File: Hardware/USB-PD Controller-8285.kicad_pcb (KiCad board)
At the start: 2 copper layers, 34 x 34 mm, 30 parts, among them J1 Conn_01x07_Male, J10 Conn_Coaxial, J2 Conn_01x04_Male, J3 Conn_01x02_Male, J4 Conn_01x02_Male, J5 Conn_01x02_Male, J6 Conn_01x02_Male, J7 Conn_01x08_Male, Q1 UMH3N, U1 ESP8285H16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

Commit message: messin' with the controller board
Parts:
- added J8: QWIIC, Connector_JST:JST_SH_BM04B-SRSS-TB_1x04-1MP_P1.00mm_Vertical, F.Cu at (91.4, 93.7)
- moved G*** 17.6 mm to (90.4, 72.9)
- moved REF** 16.6 mm to (108.0, 73.5)
- moved C5 1.36 mm to (92.3, 87.8), turned to 180 degrees
- moved C8 1.00 mm to (87.8, 80.0)
- moved R6 0.06 mm to (94.9, 98.4)
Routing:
- net SDA: track 12.8 -> 24.7 mm
- net SCL: track 17.8 -> 26.4 mm
- net RST: track 31.9 -> 39.2 mm
- net +3V3: track 84.0 -> 89.7 mm, vias 3 -> 4
- net IO0: track 21.5 -> 23.0 mm
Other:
- board text added: "(AFC)"

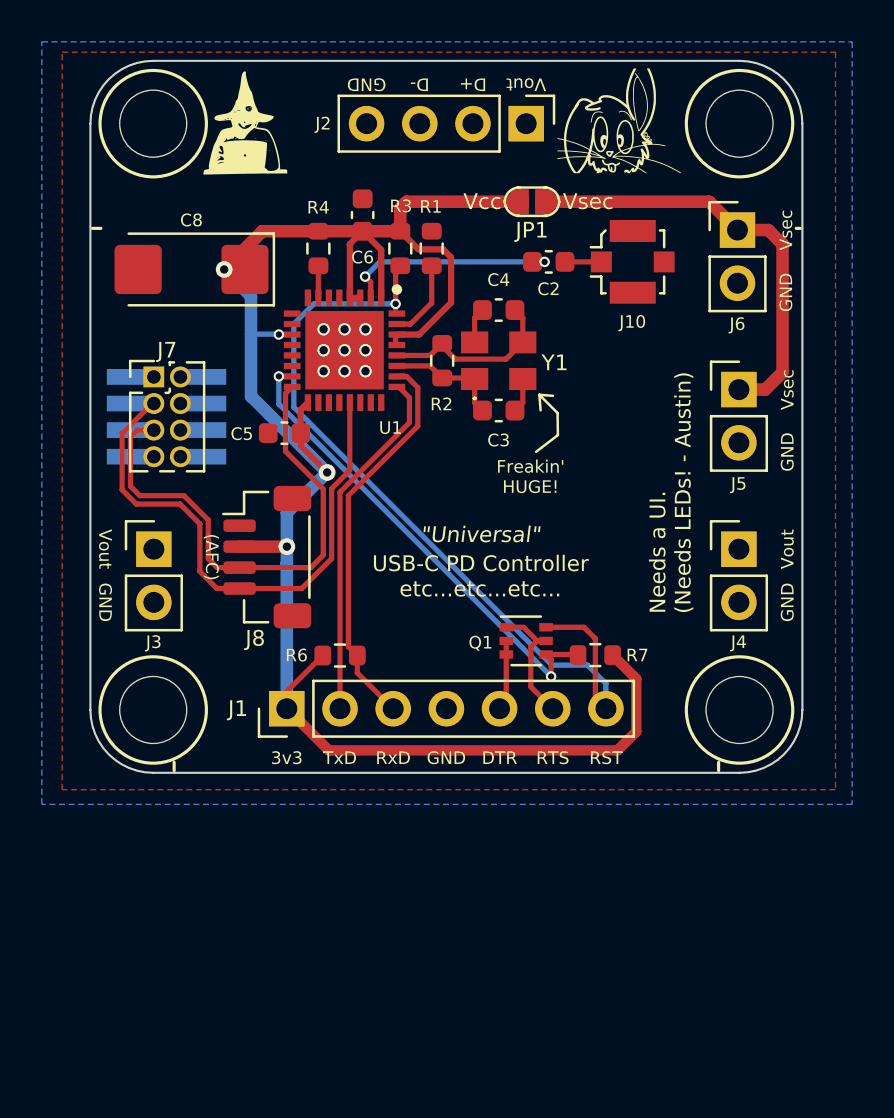
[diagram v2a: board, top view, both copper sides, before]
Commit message: aaarrrggg... RABBITS! Now there's a programmer board.
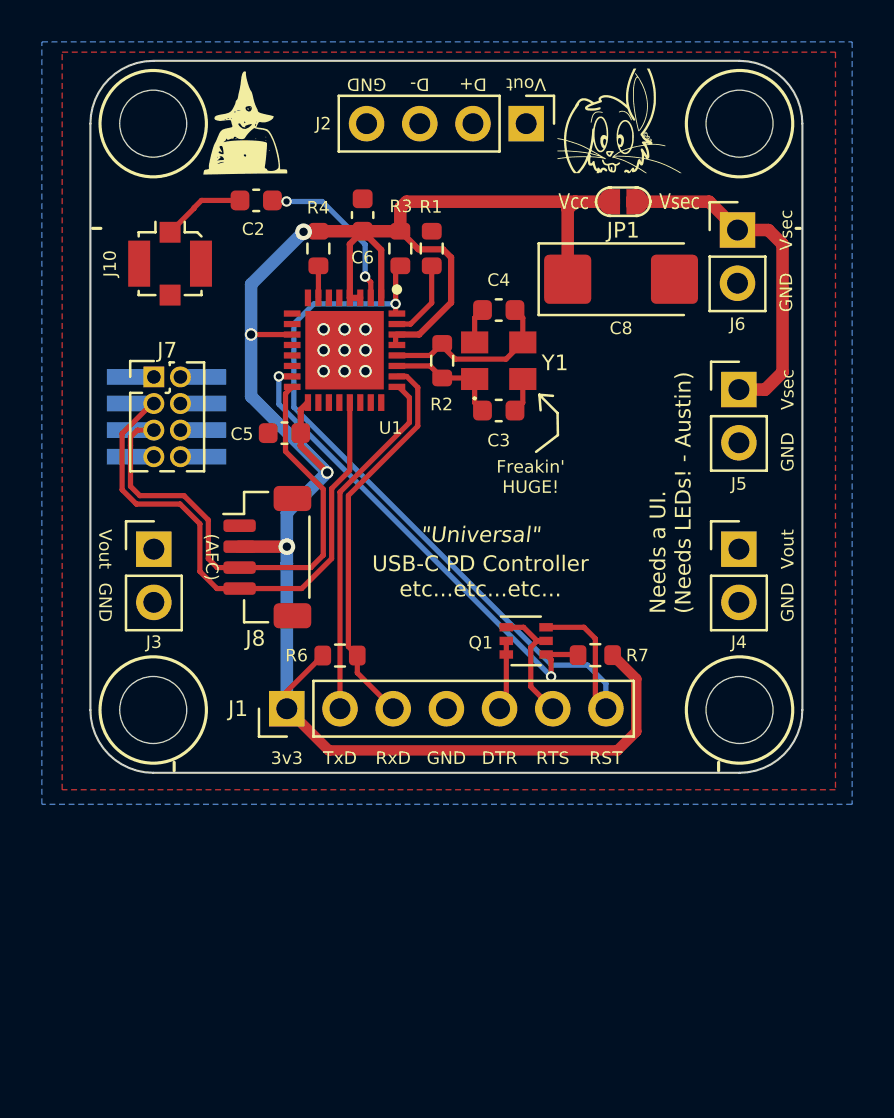
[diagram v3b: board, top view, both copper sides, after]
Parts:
- moved J10 22.1 mm to (86.8, 79.7), turned to 180 degrees
- moved C8 20.5 mm to (108.3, 80.4), turned to 0 degrees
- moved C2 14.3 mm to (90.9, 76.7), turned to 180 degrees
- moved JP1 4.36 mm to (108.4, 76.7)
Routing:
- net +3V3: track 89.7 -> 94.9 mm
- net Vsec: track 20.7 -> 16.3 mm
- net /LNA: track 9.99 -> 7.27 mm
- net Net-(C2-Pad2): track 1.73 -> 3.98 mm

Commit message: Documentation...
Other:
- board text added: "QWIIC"
- board text removed: "(AFC)"
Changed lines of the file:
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@@
     (property "exclude_from_bom" "")
     (attr smd exclude_from_bom)
-    (fp_text reference "J10" (at 2.869224 0 90) (layer "F.SilkS")
+    (fp_text reference "J10" (at -0.020454 2.740556 180) (layer "F.SilkS")
       (effects (font (size 0.6 0.6) (thickness 0.15)))
     )
@@
     (attr smd)
     (fp_text reference "Y1" (at 2.687129 0.106632) (layer "F.SilkS")
-      (effects (font (size 0.75 0.75) (thickness 0.1875)))
+      (effects (font (size 0.6 0.6) (thickness 0.15)))
     )
     (fp_text value "26.000MHz" (at 0 0.225) (layer "F.SilkS") hide
@@
     (effects (font (size 0.6 0.6) (thickness 0.125)))
   )
-  (gr_text "(AFC)" (at 88.8 93.7 270) (layer "F.SilkS")
+  (gr_text "QWIIC" (at 88.8 93.7 270) (layer "F.SilkS")
     (effects (font (size 0.6 0.6) (thickness 0.15)))
   )

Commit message: Tinkerin' + RESET & LED on Programmer...
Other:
- board text added: "NerdMage Modules ${TITLE} (v${REVISION})"
- board text removed: "NerdMage Modules (v0.0.1)"
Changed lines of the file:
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@@
   (paper "A4")
   (title_block
-    (title "USB-C PD Controller")
-    (rev "0.0.1")
+    (title "USB-PD Controller")
+    (rev "0.0.2")
     (company "The Nerd Mage")
   )
@@
   (gr_line (start 86 104) (end 114 104) (layer "Edge.Cuts") (width 0.1))
   (gr_arc (start 117 101) (mid 116.12132 103.12132) (end 114 104) (layer "Edge.Cuts") (width 0.1))
-  (gr_text "NerdMage Modules (v0.0.1)" (at 100 74.8) (layer "B.SilkS")
+  (gr_text "NerdMage Modules\n${TITLE} (v${REVISION})" (at 100 76) (layer "B.SilkS")
     (effects (font (size 1 1) (thickness 0.15)) (justify mirror))
   )
@@
     (effects (font (size 0.6 0.6) (thickness 0.125)) (justify mirror))
   )
-  (gr_text "S. A. Miller 2023" (at 100 99) (layer "B.SilkS")
+  (gr_text "S. A. Miller 2023" (at 100 79) (layer "B.SilkS")
     (effects (font (size 1 1) (thickness 0.15)) (justify mirror))
   )

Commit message: Expanding on the Controller Board functionality...
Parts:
- removed J8: QWIIC, Connector_JST:JST_SH_BM04B-SRSS-TB_1x04-1MP_P1.00mm_Vertical
- added J9: QWIIC_Stackable, Tinker:QWIIC_Stackable, F.Cu at (87.0, 80.0)
- added SW1: SW_Push, Tinker:SW_Push_TS273014TP, F.Cu at (109.0, 93.3)
- moved J10 23.4 mm to (109.0, 87.0)
- moved C2 18.5 mm to (108.2, 83.1), turned to 0 degrees
- moved C5 1.07 mm to (91.2, 87.7), turned to -90 degrees
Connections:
- J7 pad 1: RESET -> IO16
- J7 pad 4: POWER_OK2 -> IO12
- J7 pad 6: POWER_OK3 -> IO13
- J7 pad 8: GPIO -> PD_GPIO
- U1 pad 13: IO15 -> PD_GPIO
- U1 pad 14: IO2 -> ALERT
- U1 pad 21: SCL -> IO6
- U1 pad 24: IO5 -> SCL
- U1 pad 9: IO14 -> ATTACH
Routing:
- net Vsec: track 16.3 -> 31.2 mm
- net ALERT: track 0.00 -> 14.0 mm, vias 0 -> 1
- net PD_GPIO: track 0.00 -> 12.9 mm, vias 0 -> 1
- net IO16: track 0.00 -> 10.3 mm, vias 0 -> 1
- net IO13: track 0.00 -> 9.20 mm, vias 0 -> 2
- net /LNA: track 7.27 -> 16.3 mm
- net IO12: track 0.00 -> 8.43 mm, vias 0 -> 2
- net ATTACH: track 0.00 -> 7.60 mm, vias 0 -> 1
- net RST: track 39.2 -> 46.7 mm
- net IO0: track 23.0 -> 28.6 mm
- net SDA: track 24.7 -> 19.6 mm
- net +3V3: track 94.9 -> 92.1 mm, vias 4 -> 3
- net SCL: track 26.4 -> 23.9 mm
- net Net-(C2-Pad2): track 3.98 -> 2.35 mm
- net GND: vias 9 -> 1
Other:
- board text added: "RESET"
- board text added: "alert"
- board text added: "attach"
- board text added: "gpio"
- board text added: "pok2"
- board text added: "pok3"
- board text added: "rst"
- board text added: "scl"
- board text added: "sda"
- board text added: "xxxxxx"

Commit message: ...
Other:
- board text added: "${TITLE}"
- board text removed: "USB-C PD Controller etc...etc...etc..."
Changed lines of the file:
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@@
     (effects (font (size 1 1) (thickness 0.15)))
   )
-  (gr_text "USB-C PD Controller\netc...etc...etc..." (at 94.437347 93.027774 45) (layer "F.SilkS")
+  (gr_text "${TITLE}" (at 94.437347 93.027774 45) (layer "F.SilkS")
     (effects (font (size 0.75 0.75) (thickness 0.15)))
   )

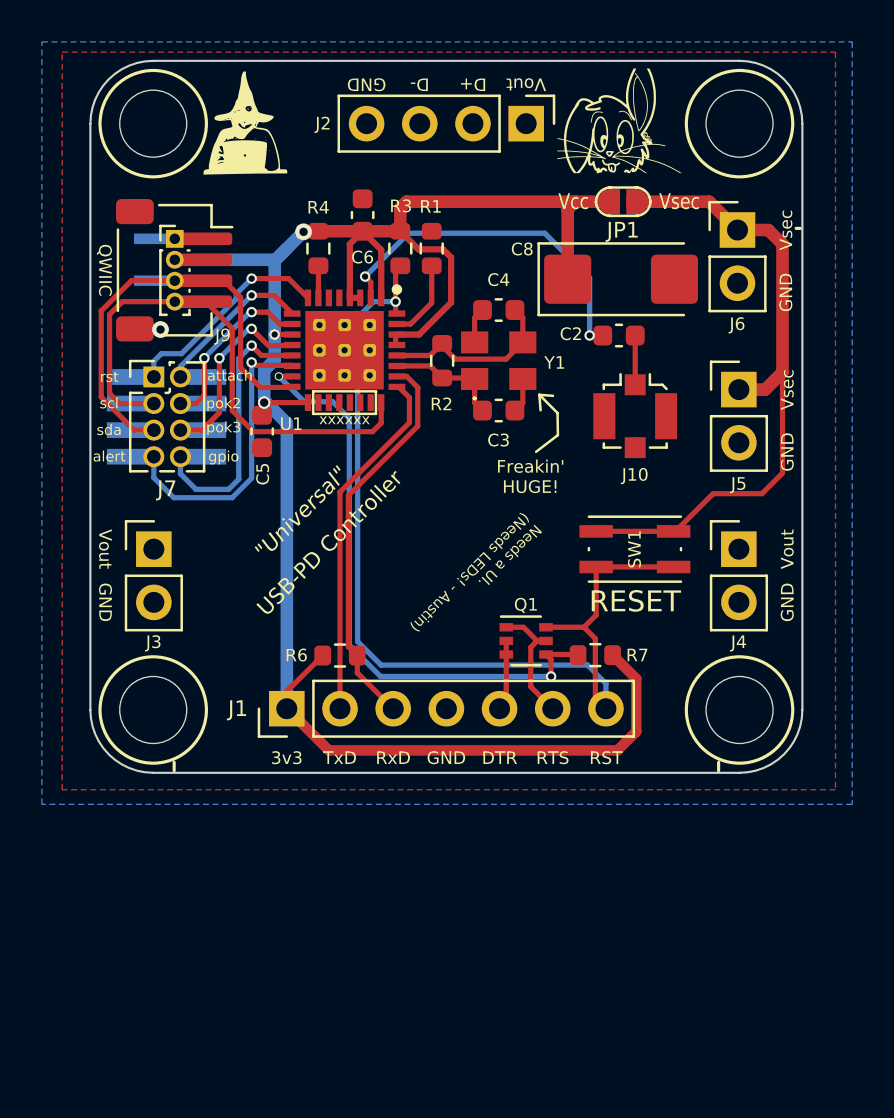
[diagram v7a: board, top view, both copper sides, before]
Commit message: Rabbit-Hole OCD... Redesigned Controller Board
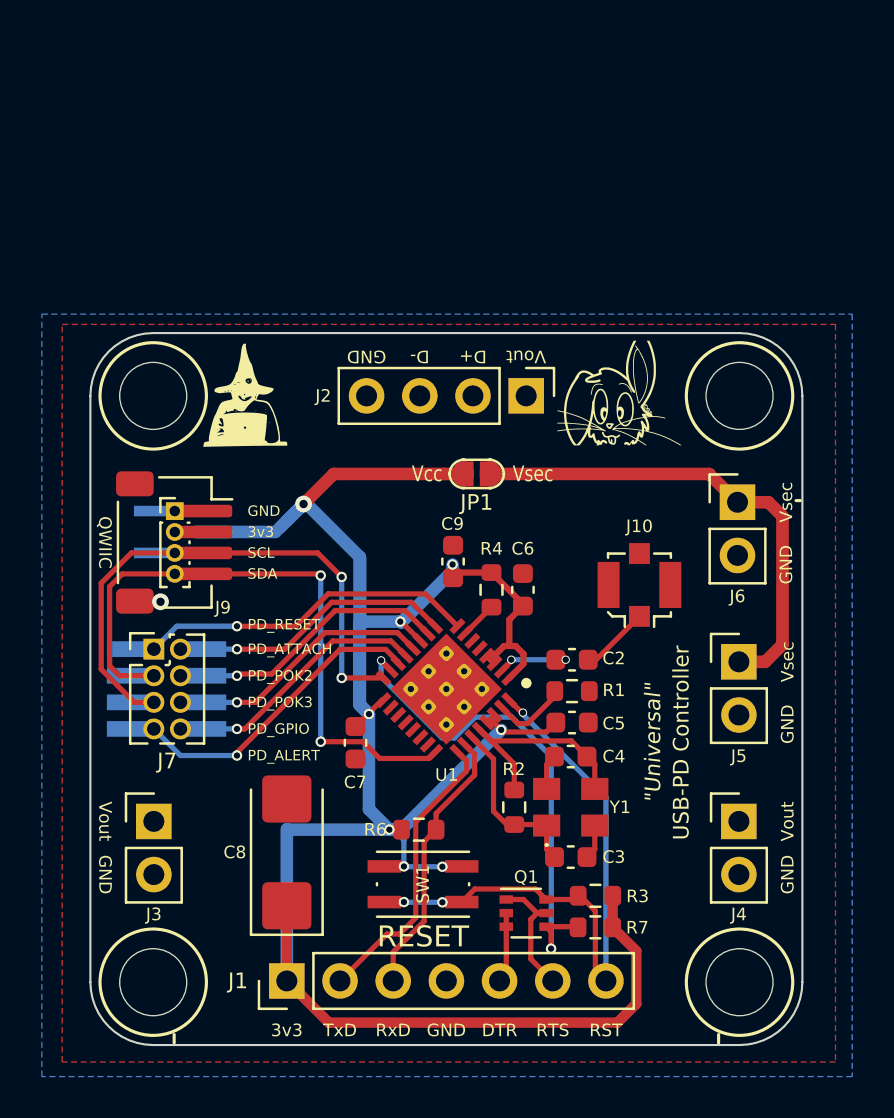
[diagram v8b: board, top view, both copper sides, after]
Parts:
- added C7: 1uf, Capacitor_SMD:C_0603_1608Metric, F.Cu at (95.7, 102.6)
- added C9: 1uf, Capacitor_SMD:C_0603_1608Metric, F.Cu at (100.3, 93.9)
- moved R3 32.3 mm to (107.1, 109.9), turned to 0 degrees
- moved C8 31.7 mm to (92.4, 107.8), turned to 90 degrees
- moved R1 22.2 mm to (106.0, 100.1), turned to 180 degrees
- moved R2 21.6 mm to (103.2, 105.6)
- moved Y1 21.6 mm to (105.9, 105.6)
- moved C3 21.6 mm to (105.9, 108.0)
- moved C4 21.6 mm to (105.9, 103.2)
- moved C5 20.3 mm to (106.0, 101.6), turned to 180 degrees
- moved C6 19.5 mm to (103.7, 95.3), turned to -90 degrees
- moved SW1 18.9 mm to (98.9, 109.3)
- moved R4 18.3 mm to (102.2, 95.3)
- moved U1 16.9 mm to (100.0, 100.0), turned to -135 degrees
- moved C2 15.6 mm to (106.0, 98.6)
- moved JP1 14.8 mm to (101.4, 89.7)
- moved G*** 13.0 mm to (90.4, 85.9)
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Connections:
- net PD_GPIO renamed IO15
- C5 pad 1: +3V3 -> GND
- C5 pad 2: GND -> +3V3
- C6 pad 1: +3V3 -> GND
- C6 pad 2: GND -> +3V3
- SW1 pad 2: Vsec -> +3V3
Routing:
- net +3V3: track 92.1 -> 113.6 mm, vias 3 -> 8
- net RST: track 46.7 -> 27.8 mm, vias 1 -> 3
- net /LNA: track 16.3 -> 3.30 mm
- net Vsec: track 31.2 -> 23.3 mm
- net IO16: track 10.3 -> 16.2 mm
- net IO1: track 18.8 -> 13.1 mm
- net SDA: track 19.6 -> 25.2 mm, vias 0 -> 2
- net SCL: track 23.9 -> 28.9 mm, vias 0 -> 2
- net ATTACH: track 7.60 -> 12.4 mm
- net IO0: track 28.6 -> 23.9 mm
- net IO12: track 8.43 -> 12.4 mm, vias 2 -> 1
- net IO3: track 17.0 -> 14.0 mm
- net /eXo: track 5.63 -> 8.37 mm
- net IO13: track 9.20 -> 11.7 mm, vias 2 -> 1
- net /eXi: track 8.67 -> 10.9 mm
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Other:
- board text added: "PD_ALERT"
- board text added: "PD_ATTACH"
- board text added: "PD_GPIO"
- board text added: "PD_POK2"
- board text added: "PD_POK3"
- board text added: "PD_RESET"
- board text added: "SCL"
- board text added: "SDA"
- board text removed: "Freakin' HUGE!"
- board text removed: "Needs a UI. (Needs LEDs! - Austin)"
- board text removed: "alert"
- board text removed: "attach"
- board text removed: "gpio"
- board text removed: "pok2"
- board text removed: "pok3"
- board text removed: "rst"
- board text removed: "scl"
- board text removed: "sda"
- board text removed: "xxxxxx"
